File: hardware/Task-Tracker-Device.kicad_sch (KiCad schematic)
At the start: 3 parts, among them SW1 SW_Push_Task_1

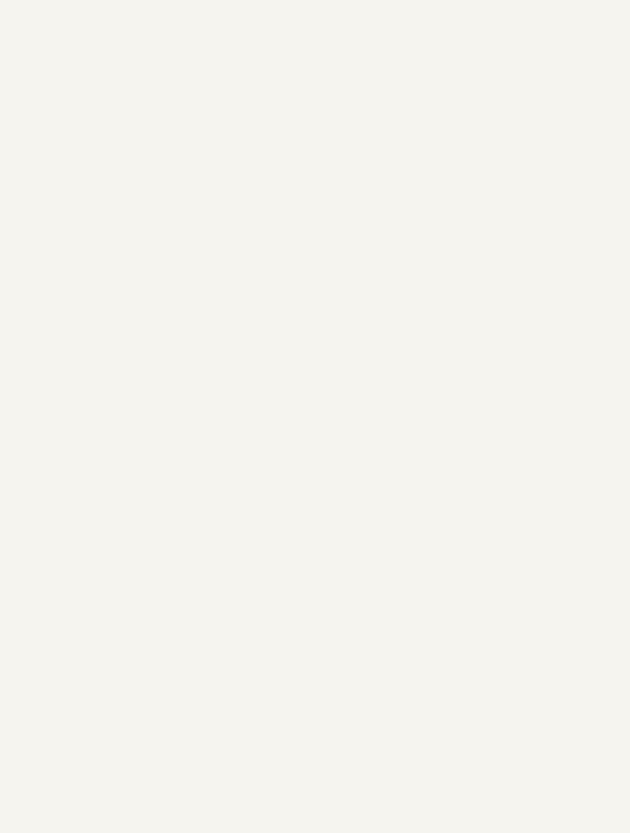
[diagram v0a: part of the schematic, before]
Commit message: Added dev-board to schematics.
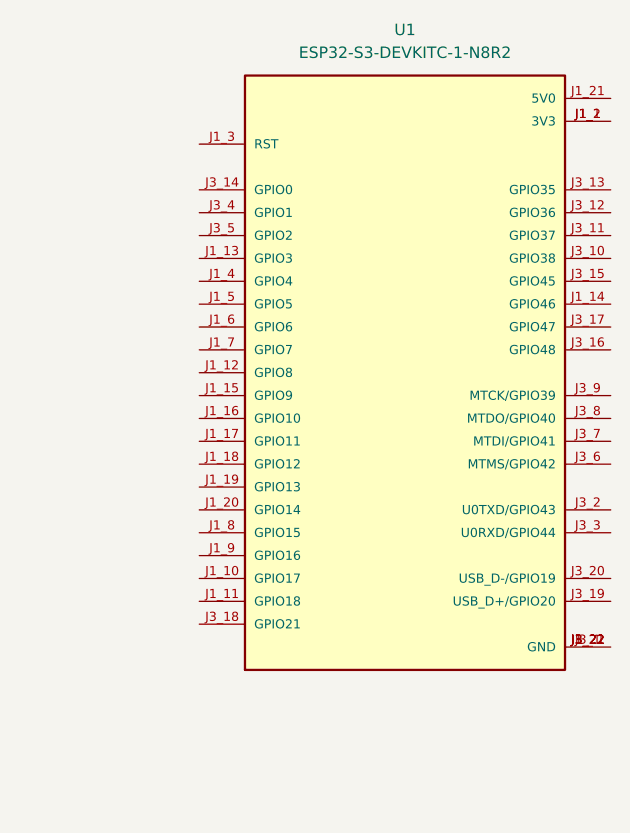
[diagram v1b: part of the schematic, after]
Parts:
- added U1: ESP32-S3-DEVKITC-1-N8R2, ESP32-S3-DEVKITC-1-N8R2:XCVR_ESP32-S3-DEVKITC-1-N8R2, symbol ESP32-S3-DEVKITC-1-N8R2:ESP32-S3-DEVKITC-1-N8R2
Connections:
- new net: U1.J1_1 (3V3), U1.J1_2 (3V3)
- new net: U1.J1_22 (GND), U1.J3_1 (GND), U1.J3_21 (GND), U1.J3_22 (GND)
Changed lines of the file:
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@@
     (stroke (width 0) (type default))
+  )
+  (symbol (lib_id "ESP32-S3-DEVKITC-1-N8R2:ESP32-S3-DEVKITC-1-N8R2") (at 247.65 60.96 0) (unit 1)
+    (in_bom yes) (on_board yes) (dnp no) (fields_autoplaced)
+    (property "Reference" "U1" (at 247.65 22.86 0)
+      (effects (font (size 1.27 1.27)))
+    )
+    (property "Value" "ESP32-S3-DEVKITC-1-N8R2" (at 247.65 25.4 0)
+      (effects (font (size 1.27 1.27)))
+    )
+    (property "Footprint" "ESP32-S3-DEVKITC-1-N8R2:XCVR_ESP32-S3-DEVKITC-1-N8R2" (at 247.65 60.96 0)
+      (effects (font (size 1.27 1.27)) (justify bottom) hide)
+    )
+    (property "Datasheet" "" (at 247.65 60.96 0)
+      (effects (font (size 1.27 1.27)) hide)
+    )
+    (property "MF" "Espressif Systems" (at 247.65 60.96 0)
+      (effects (font (size 1.27 1.27)) (justify bottom) hide)
+    )
+    (property "Description" "\nWiFi Development Tools - 802.11 (Engineering Samples Only) ESP32-S3 General-Purpose Development Board, ESP32-S3-WROOM-1-N8R2, with Pin Header\n" (at 247.65 60.96 0)
+      (effects (font (size 1.27 1.27)) (justify bottom) hide)
+    )
+    (property "Package" "None" (at 247.65 60.96 0)
+      (effects (font (size 1.27 1.27)) (justify bottom) hide)
+    )
+    (property "Price" "None" (at 247.65 60.96 0)
+      (effects (font (size 1.27 1.27)) (justify bottom) hide)
+    )
+    (property "Check_prices" "https://www.snapeda.com/parts/ESP32-S3-DEVKITC-1-N8R2/Espressif+Systems/view-part/?ref=eda" (at 247.65 60.96 0)
+      (effects (font (size 1.27 1.27)) (justify bottom) hide)
+    )
+    (property "STANDARD" "Manufacturer Recommendations" (at 247.65 60.96 0)
+      (effects (font (size 1.27 1.27)) (justify bottom) hide)
+    )
+    (property "PARTREV" "V1" (at 247.65 60.96 0)
+      (effects (font (size 1.27 1.27)) (justify bottom) hide)
+    )
+    (property "SnapEDA_Link" "https://www.snapeda.com/parts/ESP32-S3-DEVKITC-1-N8R2/Espressif+Systems/view-part/?ref=snap" (at 247.65 60.96 0)
+      (effects (font (size 1.27 1.27)) (justify bottom) hide)
+    )
+    (property "MP" "ESP32-S3-DEVKITC-1-N8R2" (at 247.65 60.96 0)
+      (effects (font (size 1.27 1.27)) (justify bottom) hide)
+    )
+    (property "Purchase-URL" "https://www.snapeda.com/api/url_track_click_mouser/?unipart_id=8918256&manufacturer=Espressif Systems&part_name=ESP32-S3-DEVKITC-1-N8R2&search_term=esp32-s3-devkitc-1-n8" (at 247.65 60.96 0)
+      (effects (font (size 1.27 1.27)) (justify bottom) hide)
+    )
+    (property "Availability" "In Stock" (at 247.65 60.96 0)
+      (effects (font (size 1.27 1.27)) (justify bottom) hide)
+    )
+    (property "MANUFACTURER" "Espressif" (at 247.65 60.96 0)
+      (effects (font (size 1.27 1.27)) (justify bottom) hide)
+    )
+    (pin "J1_1")
+    (pin "J1_10")
+    (pin "J1_11")
+    (pin "J1_12")
+    (pin "J1_13")
+    (pin "J1_14")
+    (pin "J1_15")
+    (pin "J1_16")
+    (pin "J1_17")
+    (pin "J1_18")
+    (pin "J1_19")
+    (pin "J1_2")
+    (pin "J1_20")
+    (pin "J1_21")
+    (pin "J1_22")
+    (pin "J1_3")
+    (pin "J1_4")
+    (pin "J1_5")
+    (pin "J1_6")
+    (pin "J1_7")
+    (pin "J1_8")
+    (pin "J1_9")
+    (pin "J3_1")
+    (pin "J3_10")
+    (pin "J3_11")
+    (pin "J3_12")
+    (pin "J3_13")
+    (pin "J3_14")
+    (pin "J3_15")
+    (pin "J3_16")
+    (pin "J3_17")
+    (pin "J3_18")
+    (pin "J3_19")
+    (pin "J3_2")
+    (pin "J3_20")
+    (pin "J3_21")
+    (pin "J3_22")
+    (pin "J3_3")
+    (pin "J3_4")
+    (pin "J3_5")
+    (pin "J3_6")
+    (pin "J3_7")
+    (pin "J3_8")
+    (pin "J3_9")
+    (instances
+      (project "Task-Tracker-Device"
+        (path "/4717b813-6ec7-44de-b704-38a51824a778"
+          (reference "U1") (unit 1)
+        )
+      )
+    )
   )
   (symbol (lib_id "Device:R") (at 86.36 95.25 90) (unit 1)
